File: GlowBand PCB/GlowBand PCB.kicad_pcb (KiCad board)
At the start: 2 copper layers, 44 x 34.4 mm, 81 parts, among them P1 Solder_Pad, P2 Solder_Pad, P3 Solder_Pad, P4 Solder_Pad, P5 Solder_Pad, P6 Solder_Pad, P7 Solder_Pad, P8 Solder_Pad, P9 Magnetic Pogopin 6pin female, SW1 TS24CA, SW2 TS24CA, SW3 TS-1185EC-C-D-B, SW4 TS-1185EC-C-D-B, U1 ESP32-WROOM-32E, U10 SN74LVC1G373DBVR, U13 AP40P05, U15 MSM261D4030H1CPM, U16 AP40P05, U17 AO3400A, U18 FS8205A, U19 TP4056, U2 FXL0530-6R8-M, U20 DW01A, U3 SN74LVC2T45DCUR, U4 TPS61032PWPR, U5 AP40P05, U6 SS54, U7 SPX3819M5-L-3-3_TR, U8 LSM6DS3TR-C, U9 AP40P05

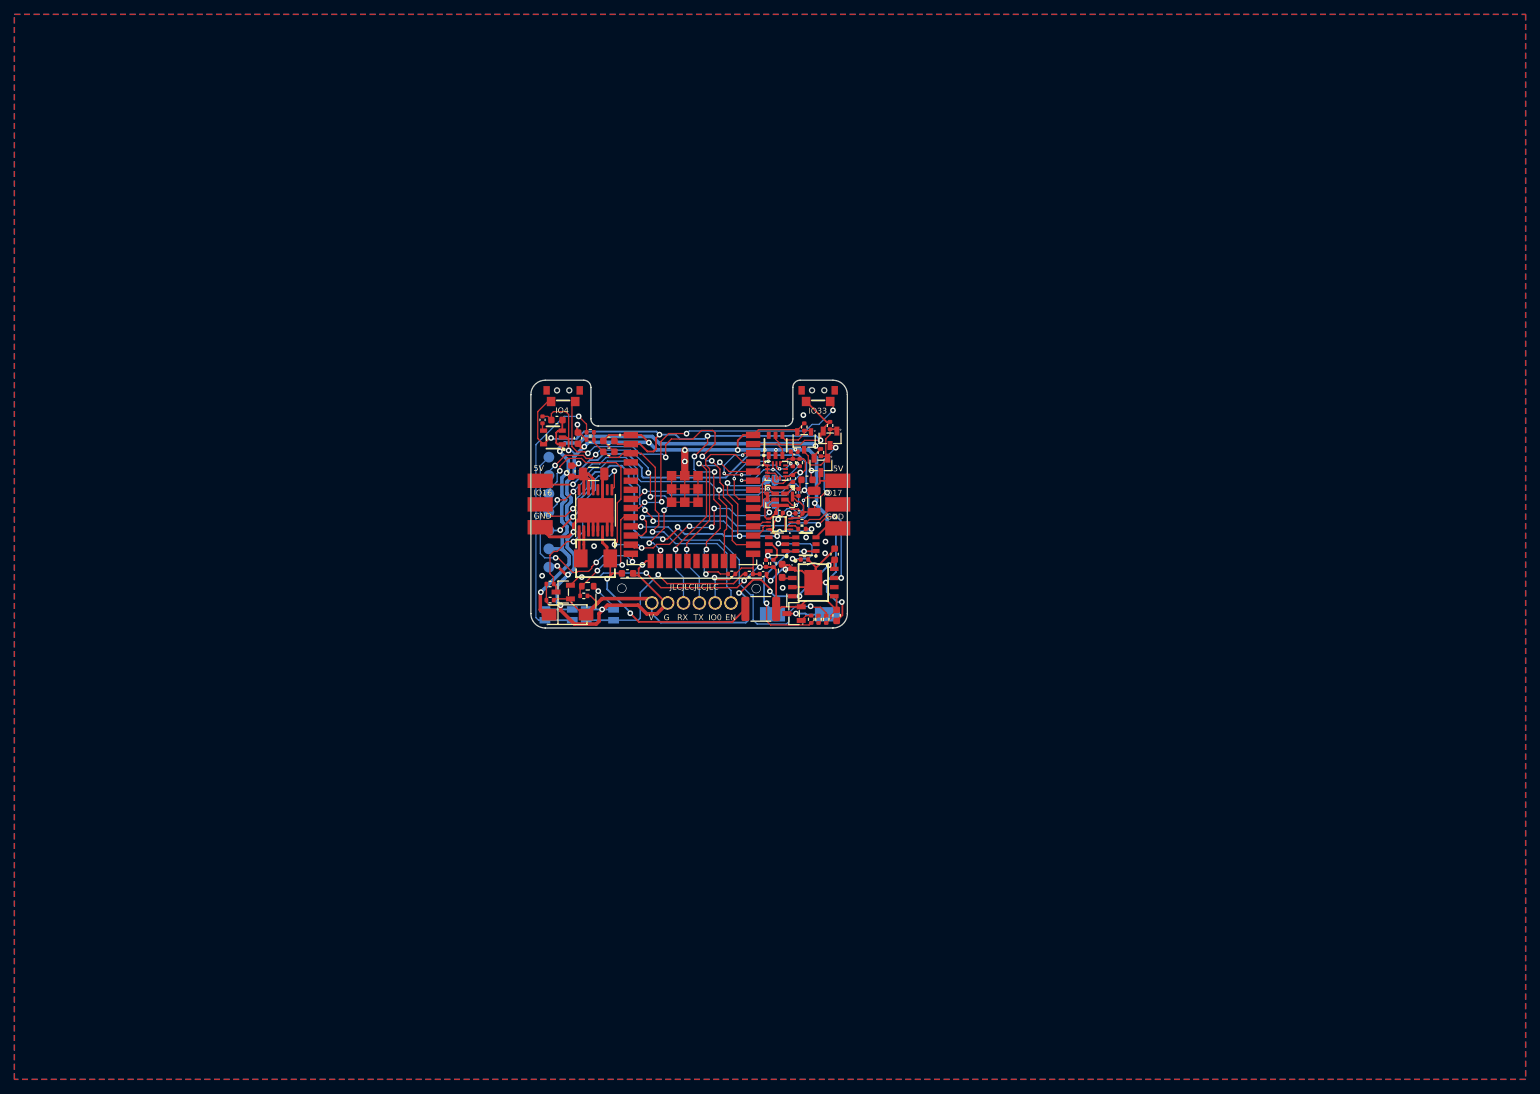
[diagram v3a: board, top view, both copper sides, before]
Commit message: updated pcb design and case prototype
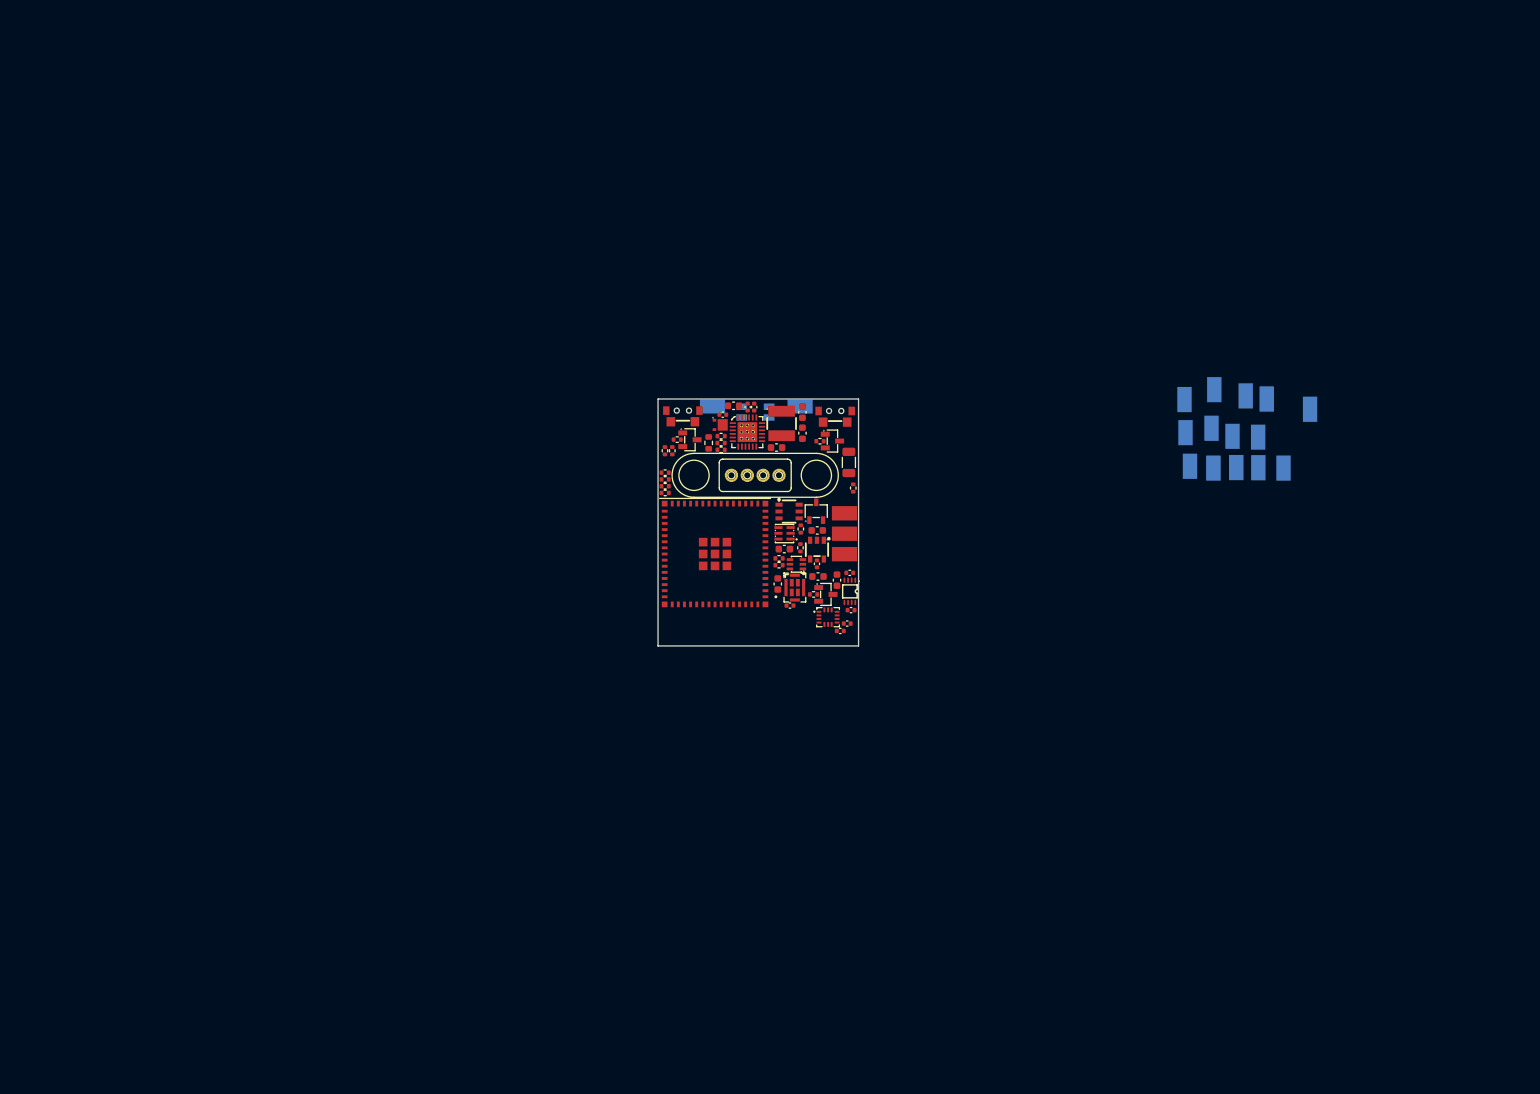
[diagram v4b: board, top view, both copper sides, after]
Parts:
- removed C20: 0.1uF, Capacitor_SMD:C_0402_1005Metric
- removed F1: BSMD1812-300-16V, Fuse:Fuse_1812_4532Metric
- removed G***: LOGO, LOGO
- removed JP1, JP2: SolderJumper_2_Bridged, Jumper:SolderJumper-2_P1.3mm_Bridged_RoundedPad1.0x1.5mm
- removed R19: 220, Resistor_SMD:R_0402_1005Metric
- removed R20, R21: 10K, Resistor_SMD:R_0402_1005Metric
- removed R22: 2K, Resistor_SMD:R_0603_1608Metric_Pad0.98x0.95mm_HandSolder
- removed R23: 100, Resistor_SMD:R_0402_1005Metric
- removed SW4: TS-1185EC-C-D-B, footprint:SW-SMD_4P-L3.7-W3.0-P1.50-LS4.7
- removed TP1, TP2, TP3, TP4, TP5, TP6, TP7: TestPoint, TestPoint:TestPoint_Pad_D1.5mm
- removed U15: MSM261D4030H1CPM, footprint:MIC-SMD_8P-L3.0-W4.0-P0.85-BL
- removed U16: AP40P05, footprint:SOT-23-3_L2.9-W1.3-P1.90-LS2.4-BR
- removed U17: AO3400A, footprint:SOT-23-3_L2.9-W1.6-P1.90-LS2.8-BR
- removed U18: FS8205A, footprint:SOT-23-6_L2.9-W1.6-P0.95-LS2.8-BR
- removed U19: TP4056, footprint:ESOP-8_L4.9-W3.9-P1.27-LS6.0-BL-EP
- removed U20: DW01A, footprint:SOT-23-6_L2.9-W1.6-P0.95-LS2.8-BL
- added B1: LP803030, footprint:LP803030, B.Cu at (119.0, 85.8)
- added C13: 0.1uF, Capacitor_SMD:C_0402_1005Metric, F.Cu at (116.2, 82.7)
- added L1: WPN4020H1R0MT, footprint:IND-SMD_L4.0-W4.0_SLW40XX, F.Cu at (106.5, 56.8)
- added P10: Solder_Pad, footprint:Solder pad, B.Cu at (172.7, 62.9)
- added P11: Solder_Pad, footprint:Solder pad, B.Cu at (166.4, 62.9)
- added P12: Solder_Pad, footprint:Solder pad, B.Cu at (169.6, 62.8)
- added P13: Solder_Pad, footprint:Solder pad, B.Cu at (166.2, 57.4)
- added P14: Solder_Pad, footprint:Solder pad, B.Cu at (163.2, 62.7)
- added P15: Solder_Pad, footprint:Solder pad, B.Cu at (176.2, 62.9)
- added P16: Solder_Pad, footprint:Solder pad, B.Cu at (162.5, 58.0)
- added P17: Solder_Pad, footprint:Solder pad, B.Cu at (179.9, 54.7)
- added P18: Solder_Pad, footprint:Solder pad, B.Cu at (172.6, 58.6)
- added P19: Solder_Pad, footprint:Solder pad, B.Cu at (173.8, 53.3)
- added P20: Solder_Pad, footprint:Solder pad, B.Cu at (162.4, 53.4)
- added R10: 100K, Resistor_SMD:R_0402_1005Metric, F.Cu at (98.1, 58.5)
- added R9: 100K, Resistor_SMD:R_0402_1005Metric, F.Cu at (110.9, 80.5)
- added REF1: RT9471DGQW, footprint:RT9471_vias_in_pad, F.Cu at (101.7, 58.0)
- added U11: SPX3819M5-L-3-3_TR, footprint:SOT-23-5_L3.0-W1.7-P0.95-LS2.8-BR, F.Cu at (111.4, 74.3)
- added U12: SK9822-EC20, footprint:LED-SMD_6P-L2.0-W2.0-P0.80-TL, F.Cu at (106.9, 72.1)
- C1: value 10uF -> 1uF; footprint Capacitor_SMD:C_0603_1608Metric -> Capacitor_SMD:C_0402_1005Metric
- C11, C2, C4: value 0.1uF -> 10uF; footprint Capacitor_SMD:C_0402_1005Metric -> Capacitor_SMD:C_0603_1608Metric
- C12: value 220uF -> 0.1uF; footprint Capacitor_SMD:C_1206_3216Metric -> Capacitor_SMD:C_0402_1005Metric
- C17: value 1uF -> 0.1uF
- C18: value 10uF -> 10nF; footprint Capacitor_SMD:C_0603_1608Metric -> Capacitor_SMD:C_0402_1005Metric
- C3: value 10uF -> 220uF; footprint Capacitor_SMD:C_0603_1608Metric -> Capacitor_SMD:C_1206_3216Metric
- C5: value 2.2uF -> 4.7uF; footprint Capacitor_SMD:C_0603_1608Metric -> Capacitor_SMD:C_0402_1005Metric
- C6: value 220uF -> 47nF; footprint Capacitor_SMD:C_1206_3216Metric -> Capacitor_SMD:C_0402_1005Metric
- C8: value 10nF -> 10uF; footprint Capacitor_SMD:C_0402_1005Metric -> Capacitor_SMD:C_0603_1608Metric
- P1, P2, P6: moved to B.Cu
- P9: value Magnetic Pogopin 6pin female -> Magnetic_Pogopin_4pin_female; footprint footprint:Magnetic Pogopin 6pin female -> footprint:Magnetic Pogopin 4pin female
- R1, R2: value 62 -> 10K
- R11: value 100K -> 160K; footprint Resistor_SMD:R_0402_1005Metric -> Resistor_SMD:R_0603_1608Metric
- R12: value 33K -> 100K
- R13: value 100K -> 62
- R16: value 100K -> 33K
- R17: value 1K -> 100K
- R18: value 220 -> 5.1K
- R3, R4, R7: value 100K -> 10K
- R5, R6: value 10K -> 100K
- R8: value 160K -> 10K; footprint Resistor_SMD:R_0603_1608Metric -> Resistor_SMD:R_0402_1005Metric
- U1: value ESP32-WROOM-32E -> SN74LVC1G373DBVR; footprint footprint:WIFI-SMD_ESP32-WROOM-32E -> footprint:SOT-23-6_L2.9-W1.6-P0.95-LS2.8-BR
- U10: value SN74LVC1G373DBVR -> MSM261D4030H1CPM; footprint footprint:SOT-23-6_L2.9-W1.6-P0.95-LS2.8-BR -> footprint:MIC-SMD_8P-L3.0-W4.0-P0.85-BL
- U13: value AP40P05 -> 74LVC2G04DW-7; footprint footprint:SOT-23-3_L2.9-W1.3-P1.90-LS2.4-BR -> footprint:SOT-363_L2.0-W1.3-P0.65-LS2.1-BR
- U2: value FXL0530-6R8-M -> PTVSHC3N12VU; footprint footprint:IND-SMD_L5.4-W5.2_FXL0530 -> footprint:DFN-3_L2.0-W2.0-P1.30-BR
- U3: value SN74LVC2T45DCUR -> AP40P05; footprint footprint:VSSOP-8_L2.4-W2.1-P0.50-LS3.2-BR -> footprint:SOT-23-3_L2.9-W1.3-P1.90-LS2.4-BR
- U4: value TPS61032PWPR -> ESP32-S3-MINI-1-N8; footprint Package_SO:HTSSOP-16-1EP_4.4x5mm_P0.65mm_EP3.4x5mm_Mask2.46x2.31mm -> footprint:ESP32-S3-MINI-1-N8
- U6: value SS54 -> AO3400A; footprint footprint:SMA_L4.4-W2.8-LS5.4-RD -> footprint:SOT-23-3_L2.9-W1.6-P1.90-LS2.8-BR
- U7: value SPX3819M5-L-3-3_TR -> AP40P05; footprint footprint:SOT-23-5_L3.0-W1.7-P0.95-LS2.8-BR -> footprint:SOT-23-3_L2.9-W1.3-P1.90-LS2.4-BR
- U8: value LSM6DS3TR-C -> SN74LVC2T45DCUR; footprint footprint:LGA-14_L3.0-W2.5-P0.50-TL -> footprint:VSSOP-8_L2.4-W2.1-P0.50-LS3.2-BR
- U9: value AP40P05 -> LSM6DS3TR-C; footprint footprint:SOT-23-3_L2.9-W1.3-P1.90-LS2.4-BR -> footprint:LGA-14_L3.0-W2.5-P0.50-TL
- moved P8 72.5 mm to (170.9, 52.9), turned to 180 degrees
- moved P7 61.5 mm to (169.1, 58.5), turned to 180 degrees
- moved P6 55.7 mm to (166.5, 52.0), turned to 180 degrees
- moved P3 42.4 mm to (115.3, 69.3), turned to -90 degrees
- moved P9 41.5 mm to (114.5, 60.9), turned to -90 degrees
- moved SW3 39.3 mm to (102.9, 55.2), turned to 0 degrees
- moved P1 37.5 mm to (109.0, 54.5), turned to -90 degrees
- moved U6 37.4 mm to (111.3, 69.0), turned to -90 degrees
- moved U5 36.5 mm to (112.6, 80.5), turned to 180 degrees
- moved C8 36.2 mm to (109.4, 58.1), turned to 90 degrees
- moved C3 33.5 mm to (115.8, 62.2), turned to 90 degrees
- moved R12 32.4 mm to (92.0, 59.0), turned to 0 degrees
- moved R18 31.6 mm to (106.1, 75.5), turned to 180 degrees
- moved C9 31.4 mm to (109.4, 55.2), turned to -90 degrees
- moved C16 30.9 mm to (111.5, 71.6), turned to 0 degrees
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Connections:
- C1 pad 1: Net-(C1-Pad1) -> -BATT
- C1 pad 2: GND -> VBUS
- C10 pad 1: GYRO VDD -> 5V AFTER MOSFET
- C10 pad 2: GND -> -BATT
- C11 pad 1: GYRO VDD -> -BATT
- C11 pad 2: GND -> EN
- C12 pad 1: 5V AFTER MOSFET -> 3.3V AFTER MOSFET
- C12 pad 2: GND -> -BATT
- C14 pad 1: GND -> -BATT
- C14 pad 2: Net-(C14-Pad2) -> 3.3V AFTER MOSFET
- C15 pad 1: GND -> -BATT
- C15 pad 2: Net-(C14-Pad2) -> 3.3V AFTER MOSFET
- C16 pad 1: GND -> -BATT
- C16 pad 2: EN -> +5V
- C17 pad 1: IO0 -> 3.3V AFTER MOSFET
- C17 pad 2: GND -> -BATT
- C18 pad 1: VBUS -> -BATT
- C18 pad 2: GND -> Net-(C18-Pad2)
- C19 pad 1: +BATT -> -BATT
- C19 pad 2: GND -> +3V3
- C2 pad 1: 5V AFTER MOSFET -> -BATT
- C2 pad 2: GND -> Net-(C2-Pad2)
- C3 pad 1: GND -> 5V AFTER MOSFET
- C3 pad 2: +3V3 -> -BATT
- C4 pad 1: 3.3V AFTER MOSFET -> -BATT
- C4 pad 2: GND -> +3V3
- C5 pad 1: GND -> REGN
- C5 pad 2: +5V -> -BATT
- C6 pad 1: +5V -> Net-(C6-Pad1)
- C6 pad 2: GND -> Net-(C6-Pad2)
- C7 pad 1: GND -> -BATT
- C7 pad 2: +5V -> +BATT
- C8 pad 1: GND -> -BATT
- C8 pad 2: Net-(C8-Pad2) -> +5V
- C9 pad 1: GND -> -BATT
- C9 pad 2: +3V3 -> +5V
- P1 pad 1: 5V AFTER MOSFET -> Net-(P1-Pad1)
- P2 pad 1: LED1 DATA OUT -> -BATT
- P3 pad 1: GND -> 5V AFTER MOSFET
- P4 pad 1: 5V AFTER MOSFET -> LED1 DATA OUT
- P5 pad 1: LED2 DATA OUT -> -BATT
- P6 pad 1: GND -> IO9/I2C SCL
- P7 pad 1: Net-(P7-Pad1) -> IO8/I2C SDA
- P8 pad 1: -BATT -> IO36/SPI SCK
- P9 pad 1: VBUS -> USB D+
- P9 pad 2: GND -> USB D-
- P9 pad 3: RXD0 -> VBUS
- P9 pad 4: TXD0 -> -BATT
- R1 pad 1: Net-(R1-Pad1) -> +3V3
- R1 pad 2: LED1 DATA OUT -> IO8/I2C SDA
- R11 pad 2: Net-(R11-Pad2) -> IO7/VBUS
- R12 pad 1: IO26/BATT VOLT -> -BATT
- R12 pad 2: +BATT -> Net-(R12-Pad2)
- R13 pad 1: -BATT -> Net-(R13-Pad1)
- R13 pad 2: IO26/BATT VOLT -> LED1 DATA OUT
- R14 pad 2: +5V -> +3V3
- R15 pad 1: GND -> +3V3
- R15 pad 2: Net-(R15-Pad2) -> IO0/BOOT
- R16 pad 1: Net-(R14-Pad1) -> IO2/BATT VOLT
- R16 pad 2: +3V3 -> +BATT
- R17 pad 1: GND -> -BATT
- R17 pad 2: Net-(R17-Pad2) -> IO2/BATT VOLT
- R18 pad 1: Net-(R18-Pad1) -> +3V3
- R2 pad 1: Net-(R2-Pad1) -> +3V3
- R2 pad 2: LED2 DATA OUT -> IO9/I2C SCL
- R3 pad 1: VBUS -> +3V3
- R3 pad 2: GND -> IO10/I2C GRYO INT
- R4 pad 1: Net-(R4-Pad1) -> +3V3
- R4 pad 2: GND -> IO11/I2C BATT IC INT
- R5 pad 1: IO21/I2C SDA -> Net-(R5-Pad1)
- R5 pad 2: GYRO VDD -> +5V
- R6 pad 1: IO22/I2C SCL -> -BATT
- R6 pad 2: GYRO VDD -> Net-(R6-Pad2)
- R7 pad 1: IO25/VBUS -> REGN
- R7 pad 2: VBUS -> Net-(R7-Pad2)
- R8 pad 1: GND -> -BATT
- R8 pad 2: IO25/VBUS -> Net-(R7-Pad2)
- SW1 pad 3: +3V3 -> -BATT
- SW1 pad 4: IO33/MAINBUTTON -> Net-(R14-Pad1)
- SW2 pad 3: +3V3 -> -BATT
- SW2 pad 4: IO4/BUTTON2 -> IO0/BOOT
- SW3 pad 1: GND -> -BATT
- SW3 pad 2: Net-(R18-Pad1) -> EN
- U1 pad 1: GND -> IO15/LED LETCH EN
- U1 pad 2: +3V3 -> -BATT
- U1 pad 3: EN -> IO16/POWERMOSFETS
- U1 pad 4: unconnected-(U1-Pad4) -> Net-(R6-Pad2)
- U1 pad 5: unconnected-(U1-Pad5) -> +3V3
- U10 pad 1: IO19/LED LETCH EN -> 3.3V AFTER MOSFET
- U10 pad 2: GND -> IO12/I2S WS
- U10 pad 3: IO23/POWERMOSFETS -> IO13/I2S SCK
- U10 pad 4: Net-(R15-Pad2) -> IO14/I2S SD
- U10 pad 5: +3V3 -> -BATT
- U10 pad 6: unconnected-(U10-Pad6) -> -BATT
- U13 pad 2: +5V -> -BATT
- U13 pad 3: 5V AFTER MOSFET -> IO0/BOOT
- U2 pad 1: Net-(C1-Pad1) -> -BATT
- U2 pad 2: Net-(U2-Pad2) -> -BATT
- U3 pad 1: 5V AFTER MOSFET -> Net-(R5-Pad1)
- U3 pad 2: Net-(R1-Pad1) -> +5V
- U3 pad 3: Net-(R2-Pad1) -> 5V AFTER MOSFET
- U4 pad 1: Net-(U2-Pad2) -> -BATT
- U4 pad 10: unconnected-(U4-Pad10) -> IO6
- U4 pad 11: GND -> IO7/VBUS
- U4 pad 12: unconnected-(U4-Pad12) -> IO8/I2C SDA
- U4 pad 13: +5V -> IO9/I2C SCL
- U4 pad 14: +5V -> IO10/I2C GRYO INT
- U4 pad 15: +5V -> IO11/I2C BATT IC INT
- U4 pad 16: unconnected-(U4-Pad16) -> IO12/I2S WS
- U4 pad 17: GND -> IO13/I2S SCK
- U4 pad 2: Net-(U2-Pad2) -> -BATT
- U4 pad 3: GND -> +3V3
- U4 pad 4: GND -> IO0/ACTIONBUTTON
- U4 pad 5: GND -> IO1/POWERBUTTON
- U4 pad 6: Net-(C1-Pad1) -> IO2/BATT VOLT
- U4 pad 7: GND -> unconnected-(U4-Pad7)
- U4 pad 8: GND -> IO4
- U4 pad 9: Net-(R4-Pad1) -> IO5
- U5 pad 1: VBUS -> Net-(R5-Pad1)
- U5 pad 2: +BATT -> +3V3
- U5 pad 3: Net-(R4-Pad1) -> 3.3V AFTER MOSFET
- U6 pad 1: +5V -> Net-(R6-Pad2)
- U6 pad 2: VBUS -> -BATT
- U7 pad 1: +5V -> Net-(R12-Pad2)
- U7 pad 2: GND -> +BATT
- U7 pad 3: +5V -> Net-(P1-Pad1)
- U8 pad 1: GND -> 5V AFTER MOSFET
- U8 pad 2: GND -> Net-(R13-Pad1)
- U8 pad 3: GND -> -BATT
- U8 pad 4: IO18/I2C INT1 -> -BATT
- U8 pad 5: GYRO VDD -> -BATT
- U8 pad 6: GND -> -BATT
- U8 pad 7: GND -> IO42/LED1
- U8 pad 8: GYRO VDD -> 3.3V AFTER MOSFET
- U9 pad 1: Net-(R11-Pad2) -> -BATT
- U9 pad 2: +BATT -> -BATT
- U9 pad 3: Net-(P7-Pad1) -> -BATT
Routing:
- net GND: track 295.9 -> 0.00 mm, vias 30 -> 0
- net +3V3: track 103.4 -> 0.00 mm, vias 9 -> 0
- net +5V: track 87.3 -> 0.00 mm, vias 4 -> 0
- net 3.3V AFTER MOSFET: track 86.9 -> 0.00 mm, vias 11 -> 0
- net 5V AFTER MOSFET: track 64.7 -> 0.00 mm, vias 3 -> 0
- net VBUS: track 57.6 -> 0.00 mm, vias 4 -> 0
- net IO14/SCK/TMS: track 55.4 -> 0.00 mm, vias 7 -> 0
- net IO4/BUTTON2: track 51.4 -> 0.00 mm, vias 4 -> 0
- net +BATT: track 51.2 -> 0.00 mm, vias 4 -> 0
- net LED1 DATA OUT: track 50.9 -> 0.00 mm, vias 4 -> 0
- net IO15/WS/TDO: track 49.0 -> 0.00 mm, vias 4 -> 0
- net IO27/BATT CHARGING: track 42.7 -> 0.00 mm, vias 4 -> 0
- net IO26/BATT VOLT: track 40.7 -> 0.00 mm, vias 2 -> 0
- net IO33/MAINBUTTON: track 40.5 -> 0.00 mm, vias 4 -> 0
- net EN: track 40.1 -> 0.00 mm, vias 1 -> 0
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- removed copper zone on B.Cu, net GND
- removed copper zone on F.Cu, net GND
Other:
- board size 44 x 34.4 mm -> 27.9 x 34.3 mm
- board text removed: "+ BATT"
- board text removed: "- BATT"
- board text removed: "3.3V OUT"
- board text removed: "30.5mm"
- board text removed: "44mm"
- board text removed: "5V"
- board text removed: "5V IN/OUT"
- board text removed: "820mA battery"
- board text removed: "BOOT"
- board text removed: "EN"
- board text removed: "G"
- board text removed: "GND"
- board text removed: "GlowBand v1.0 beta 2"
- board text removed: "Gyroscope on"
- board text removed: "IO0"
- board text removed: "IO12/TDI"
- board text removed: "IO13/TCK"
- board text removed: "IO14/SCK/TMS"
- board text removed: "IO15/WS/TDO"
- board text removed: "IO16"
- board text removed: "IO17"
- board text removed: "IO33"
- board text removed: "IO4"
- board text removed: "JLCJLCJLCJLC"
- board text removed: "Microphone on"
- board text removed: "Place battery here. Make sure this PCB side is completely flat and cannot damage the battery."
- board text removed: "RESET"
- board text removed: "RX"
- board text removed: "TX"
- board text removed: "V"
- board text removed: "https://bit.ly/ 3O7S2Tk"
